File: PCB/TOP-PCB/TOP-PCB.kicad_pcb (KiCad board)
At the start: 2 copper layers, 104 x 80.6 mm, 75 parts, among them J1 12402012E212A, J2 S2B-PH-K-SLFSN, J3 Conn_01x03_Pin, J5 Conn_01x12_Pin, Q2 NPN, SW2 PTS810_SJM_250_SMTR_LFS, SW3 PTS810_SJM_250_SMTR_LFS, U1 ESP32-S3, U10 LP38691SD-3.3, U11 BME688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

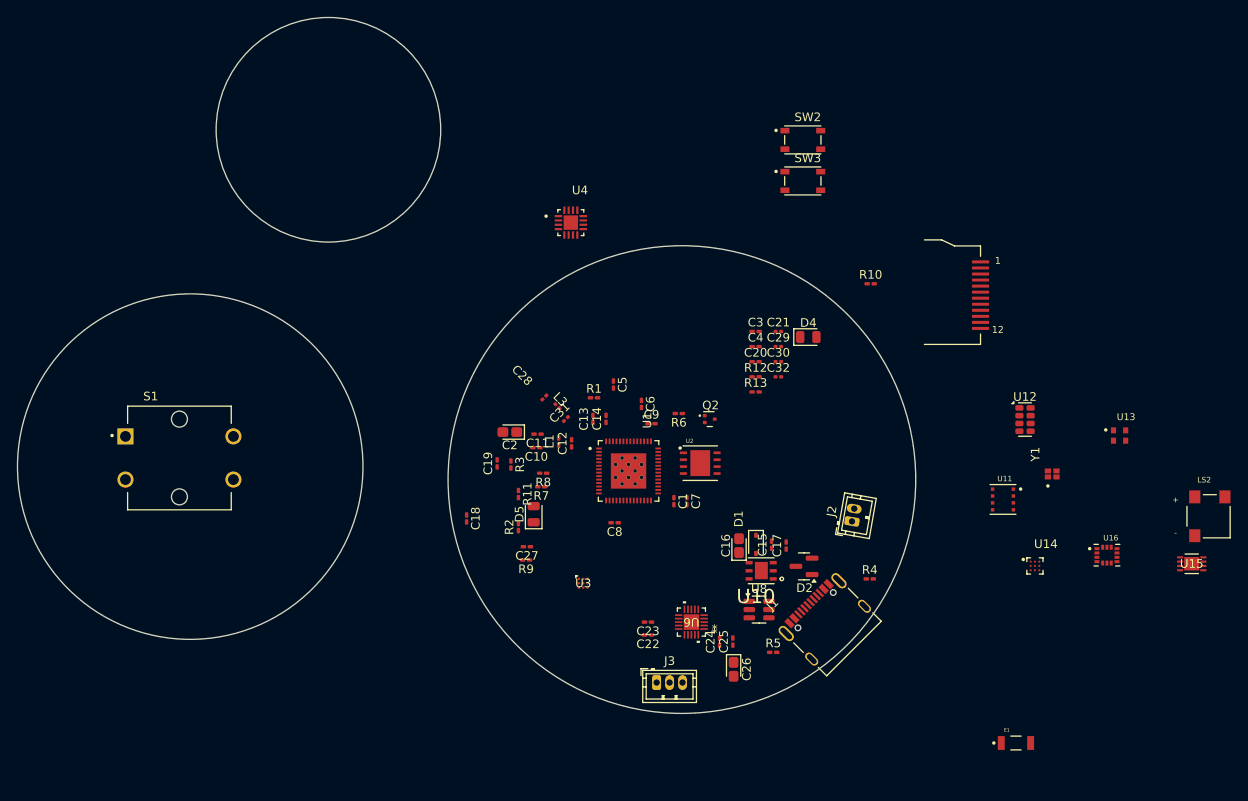
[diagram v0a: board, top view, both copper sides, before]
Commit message: re organization of top and bottom pcb
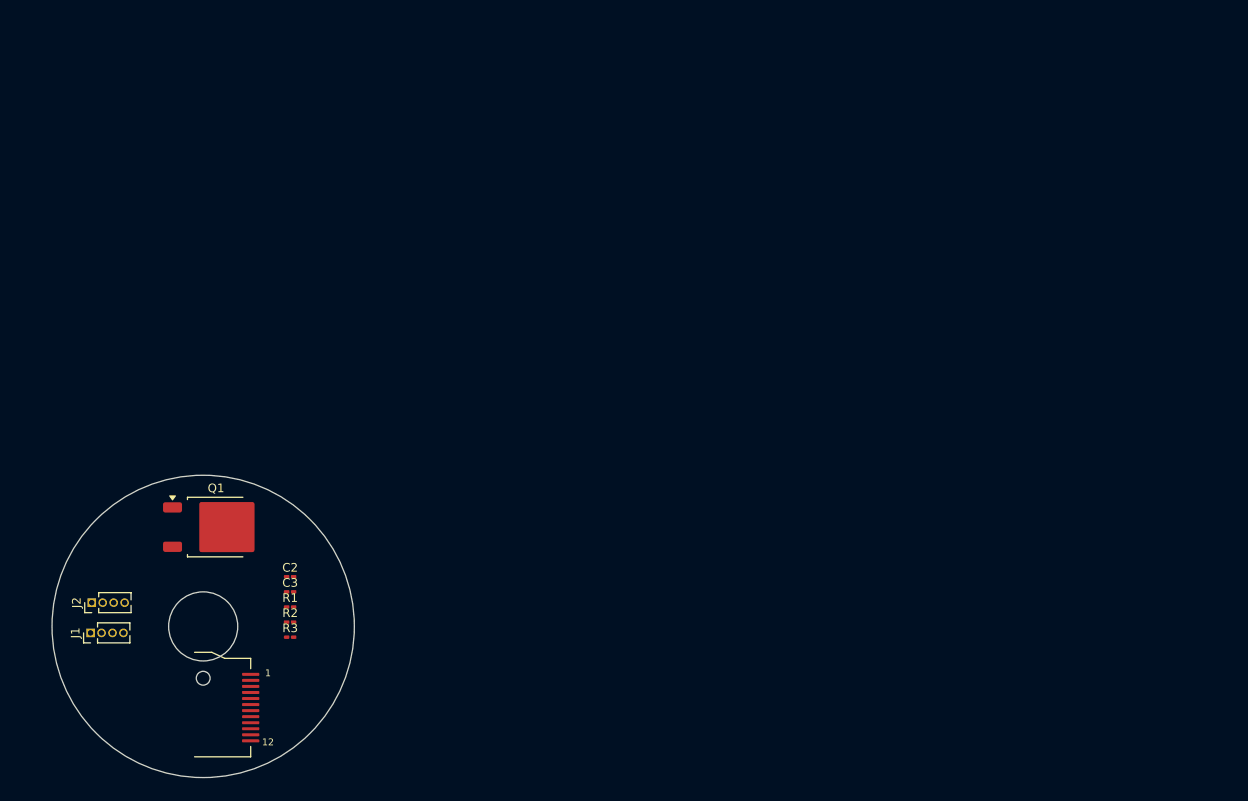
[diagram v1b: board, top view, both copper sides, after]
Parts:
- removed C1, C11, C14, C15, C17: 1 uF, Capacitor_SMD:C_0201_0603Metric_Pad0.64x0.40mm_HandSolder
- removed C10, C12, C18, C19, C20, C22, C23, C24, C25, C27, C4, C7, C8, C9: 0.1 uF, Capacitor_SMD:C_0201_0603Metric_Pad0.64x0.40mm_HandSolder
- removed C13: 10 nF, Capacitor_SMD:C_0201_0603Metric_Pad0.64x0.40mm_HandSolder
- removed C16: 10 uF, Capacitor_Tantalum_SMD:CP_EIA-1608-08_AVX-J_HandSolder
- removed C21, C29: 1 uF, Capacitor_SMD:C_0201_0603Metric
- removed C26: 22 uF, Capacitor_Tantalum_SMD:CP_EIA-1608-08_AVX-J_HandSolder
- removed C28: 1.8 pF, Capacitor_SMD:C_0201_0603Metric
- removed C30, C32: 4.7 uF, Capacitor_SMD:C_0201_0603Metric
- removed C31: 1.2 pF, Capacitor_SMD:C_0201_0603Metric
- removed C5, C6: 6 pF, Capacitor_SMD:C_0201_0603Metric_Pad0.64x0.40mm_HandSolder
- removed D1: SD03_SOD323, Diode_SMD:D_SOD-323
- removed D2: BAT54C, Package_TO_SOT_SMD:SOT-23
- removed D4, D5: LED, LED_SMD:LED_0805_2012Metric
- removed E1: AMCA31-2R450G-S1F-T3, AMCA31_2R450G_S1F_T3:XDCR_AMCA31-2R450G-S1F-T3
- removed J5: Conn_01x12_Pin, GC9A01:GC9A01Round1.28
- removed L1: 2.0 nH, Inductor_SMD:L_0201_0603Metric_Pad0.64x0.40mm_HandSolder
- removed L3: 2.4 nH, Inductor_SMD:L_0201_0603Metric
- removed LS2: CMT-0525-75-SMT-TR, CMT_0525_75_SMT_TR:XDCR_CMT-0525-75-SMT-TR
- removed Q2: NPN, Package_TO_SOT_SMD:SOT-723
- removed R10: 2.2 K, Resistor_SMD:R_0201_0603Metric_Pad0.64x0.40mm_HandSolder
- removed R11: 220, Resistor_SMD:R_0201_0603Metric_Pad0.64x0.40mm_HandSolder
- removed R12, R13: 470, Resistor_SMD:R_0201_0603Metric_Pad0.64x0.40mm_HandSolder
- removed R4, R5, R6: 5 K, Resistor_SMD:R_0201_0603Metric_Pad0.64x0.40mm_HandSolder
- removed R7, R8, R9: 10 K, Resistor_SMD:R_0201_0603Metric_Pad0.64x0.40mm_HandSolder
- removed S1: B3F-4055, B3F_4055:SW_B3F-4055
- removed SW2, SW3: PTS810_SJM_250_SMTR_LFS, PTS810SJM250SMTR_LFS:SW_PTS810_SJM_250_SMTR_LFS
- removed U1: ESP32-S3, ESP32_S3:IC_ESP32-S3
- removed U10: LP38691SD-3.3, LP38691SD_3_3_NOPB:DFN300X300X80-7N
- removed U11: BME688, BME688:IC_BME688
- removed U12: RV-3028-C7_32.768KHZ_1PPM-TA-QC, Package_SON:MicroCrystal_C7_SON-8_1.5x3.2mm_P0.9mm
- removed U13: LTR-329ALS-01, LTR_329ALS_01:IC_LTR-329ALS-01
- removed U14: BQ27427YZFR, BQ27427YZFR:IC_BQ27427YZFR
- removed U15: MCP73832T-2ACI/MC, MCP73832T:DFN8_2x3MC_MCH-L
- removed U16: LSM6DSO32TR, LSM6DSO32TR:XDCR_LSM6DSO32TR
- removed U2: MX25R6435FZAIH0, MX25R6435FZAIH0:SON80P400X400X60-9N
- removed U3: DRV2605LYZFR, DRV2605LYZFR:YZF0009ADAD
- removed U4: MLX90393SLW-ABA-011-RE, MLX90393SLW_ABA_011_RE:QFN50P300X300X100-17N
- removed U6: TMC6300-LA-T, tcm6300:21-100586_K2033&plus_1C_ADI-M
- removed U8: USBLC6-2SC6, Package_TO_SOT_SMD:SOT-23-6
- removed Y1: ABM12W-40.0000MHZ-8-B1U-T3, ABM12W_40_0000MHZ_8_B1U_T3:XTAL_ABM12W-40.0000MHZ-8-B1U-T3
- added Q1: QM6006D, Package_TO_SOT_SMD:TO-252-2, F.Cu at (152.0, 89.0)
- C2: value 10 uF -> 22 uF; footprint Capacitor_Tantalum_SMD:CP_EIA-1608-08_AVX-J_HandSolder -> Capacitor_SMD:C_0201_0603Metric_Pad0.64x0.40mm_HandSolder
- C3: value 0.1 uF -> 22 uF
- J1: value 12402012E212A -> Conn_01x04_Pin; footprint 12402012E212A:AMPHENOL_12402012E212A -> Connector_PinHeader_1.27mm:PinHeader_1x04_P1.27mm_Vertical
- J2: value S2B-PH-K-SLFSN -> Conn_01x04_Pin; footprint Connector_JST:JST_ZH_B2B-ZR_1x02_P1.50mm_Vertical -> Connector_PinHeader_1.27mm:PinHeader_1x04_P1.27mm_Vertical
- J3: value Conn_01x03_Pin -> Conn_01x12_Pin; footprint Connector_JST:JST_ZH_B3B-ZR_1x03_P1.50mm_Vertical -> LCD_GC9A01:GC9A01Round1.28
- R1: value 0 -> 22R
- R2, R3: value 5 K -> 22R
- moved J2 88.5 mm to (137.6, 97.8), turned to 90 degrees
- moved J1 86.6 mm to (137.5, 101.2), turned to 90 degrees
- moved C3 61.8 mm to (160.6, 96.5)
- moved J3 47.1 mm to (156.0, 109.9)
- moved R1 42.7 mm to (160.6, 98.2)
- moved R3 32.4 mm to (160.6, 101.8), turned to 0 degrees
- moved C2 30.5 mm to (160.6, 94.8), turned to 0 degrees
- moved R2 28.6 mm to (160.6, 100.0), turned to 0 degrees
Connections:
- J2 pad 1: +BATT -> nCS
- J2 pad 2: GND -> SCK
- J3 pad 1: U -> GND
- J3 pad 2: V -> LEDK
- J3 pad 3: W -> LEDA
- R1 pad 1: Net-(C5-Pad2) -> +3.3V
- R1 pad 2: XTAL_P -> LEDA
- R2 pad 1: +3.3V -> BACKLIGH_EN
- R2 pad 2: Boot -> Net-(Q1-G)
- R3 pad 1: +3.3V -> Net-(Q1-G)
- R3 pad 2: Reset -> GND
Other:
- board size 104 x 80.6 mm -> 35 x 35 mm

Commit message: TOP-PCB ready
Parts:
- moved R2 15.9 mm to (145.7, 94.5)
- moved R3 15.4 mm to (146.0, 96.7), turned to -90 degrees
- moved J3 12.9 mm to (165.0, 100.6), turned to 180 degrees
- moved C2 6.54 mm to (162.2, 101.1), turned to 90 degrees
- moved C3 5.73 mm to (163.2, 101.6), turned to 90 degrees
- moved R1 5.04 mm to (162.2, 103.0), turned to -90 degrees
- moved J2 4.52 mm to (137.2, 102.2)
- moved J1 3.51 mm to (137.2, 97.8)
- moved Q1 1.56 mm to (150.6, 89.7), turned to 90 degrees
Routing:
- net DC: track 0.00 -> 49.0 mm
- net nCS: track 0.00 -> 48.9 mm
- net SCK: track 0.00 -> 43.2 mm
- net +3.3V: track 0.00 -> 37.4 mm, vias 0 -> 3
- net MOSI: track 0.00 -> 37.3 mm
- net nRESET: track 0.00 -> 30.6 mm
- net LEDK: track 0.00 -> 25.8 mm, vias 0 -> 2
- net GND: track 0.00 -> 10.5 mm, vias 0 -> 5
- net BACKLIGH_EN: track 0.00 -> 7.73 mm
- net Net-(Q1-G): track 0.00 -> 4.11 mm
- net LEDA: track 0.00 -> 2.92 mm
- added copper zone on B.Cu, net GND
